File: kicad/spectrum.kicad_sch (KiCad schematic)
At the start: 114 parts

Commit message: Pre-amplifier
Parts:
- added C? (x3): 0.1uF, symbol Device:C_Small
- added C? (x3): 470uF, symbol Device:C_Polarized_Small_US
- added C?: 10uF, symbol Device:C_Small
- added R? (x4): 10K, symbol Device:R_US
- added U? (x3): Opamp_Dual, symbol Device:Opamp_Dual
- added U?: L7805, symbol Regulator_Linear:L7805
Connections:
- net +5V: now also C?.1, C?.1, C?.2, C?.2, R?.1, U?.3 (OUT), U?.8 (V+)
- net GNDREF: now also C?.1, C?.1, C?.2, C?.2, R?.2, U?.2 (GND), U?.4 (V-)
- new net: R?.1, U?.1
- new net: R?.1, R?.2, U?.2 (-)
- new net: C?.2, R?.2
- new net VDD: U?.1 (IN)
- new net VGND: C?.1, C?.1, C?.2, C?.2, R?.1, R?.2, U?.3 (+)
- new net Vin: C?.1

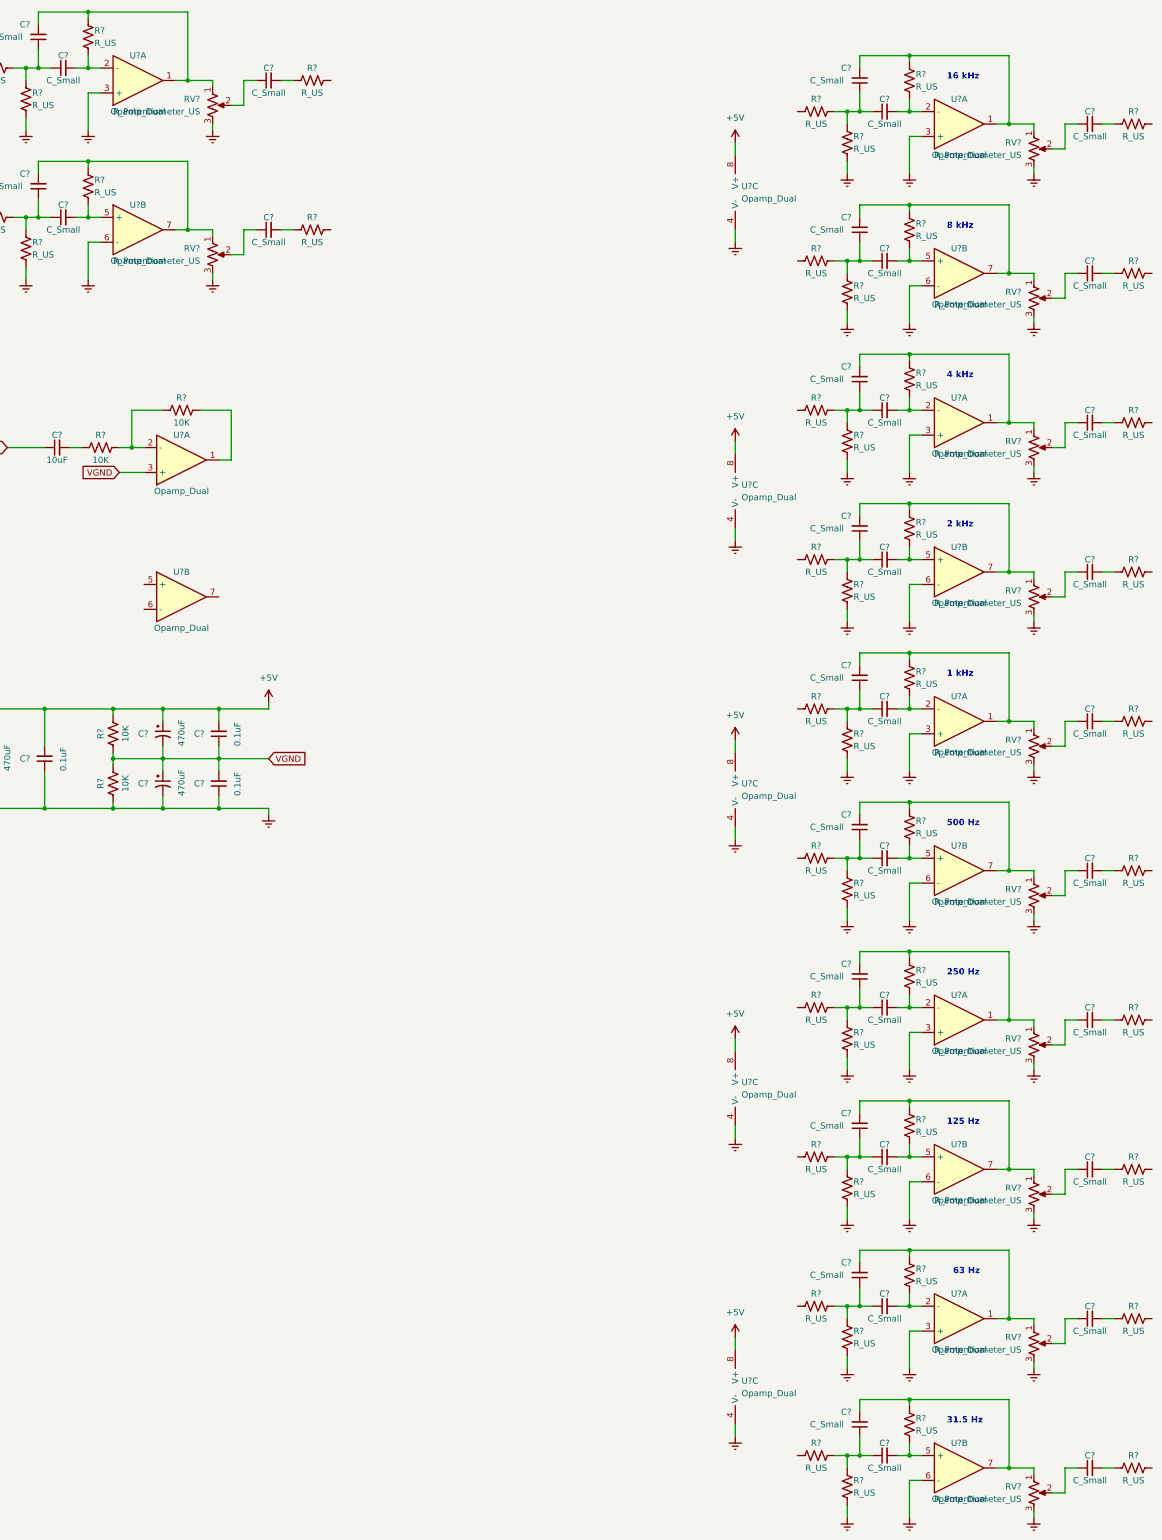
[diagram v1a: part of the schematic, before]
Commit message: Fix swapped BPF input terminals to be inverting
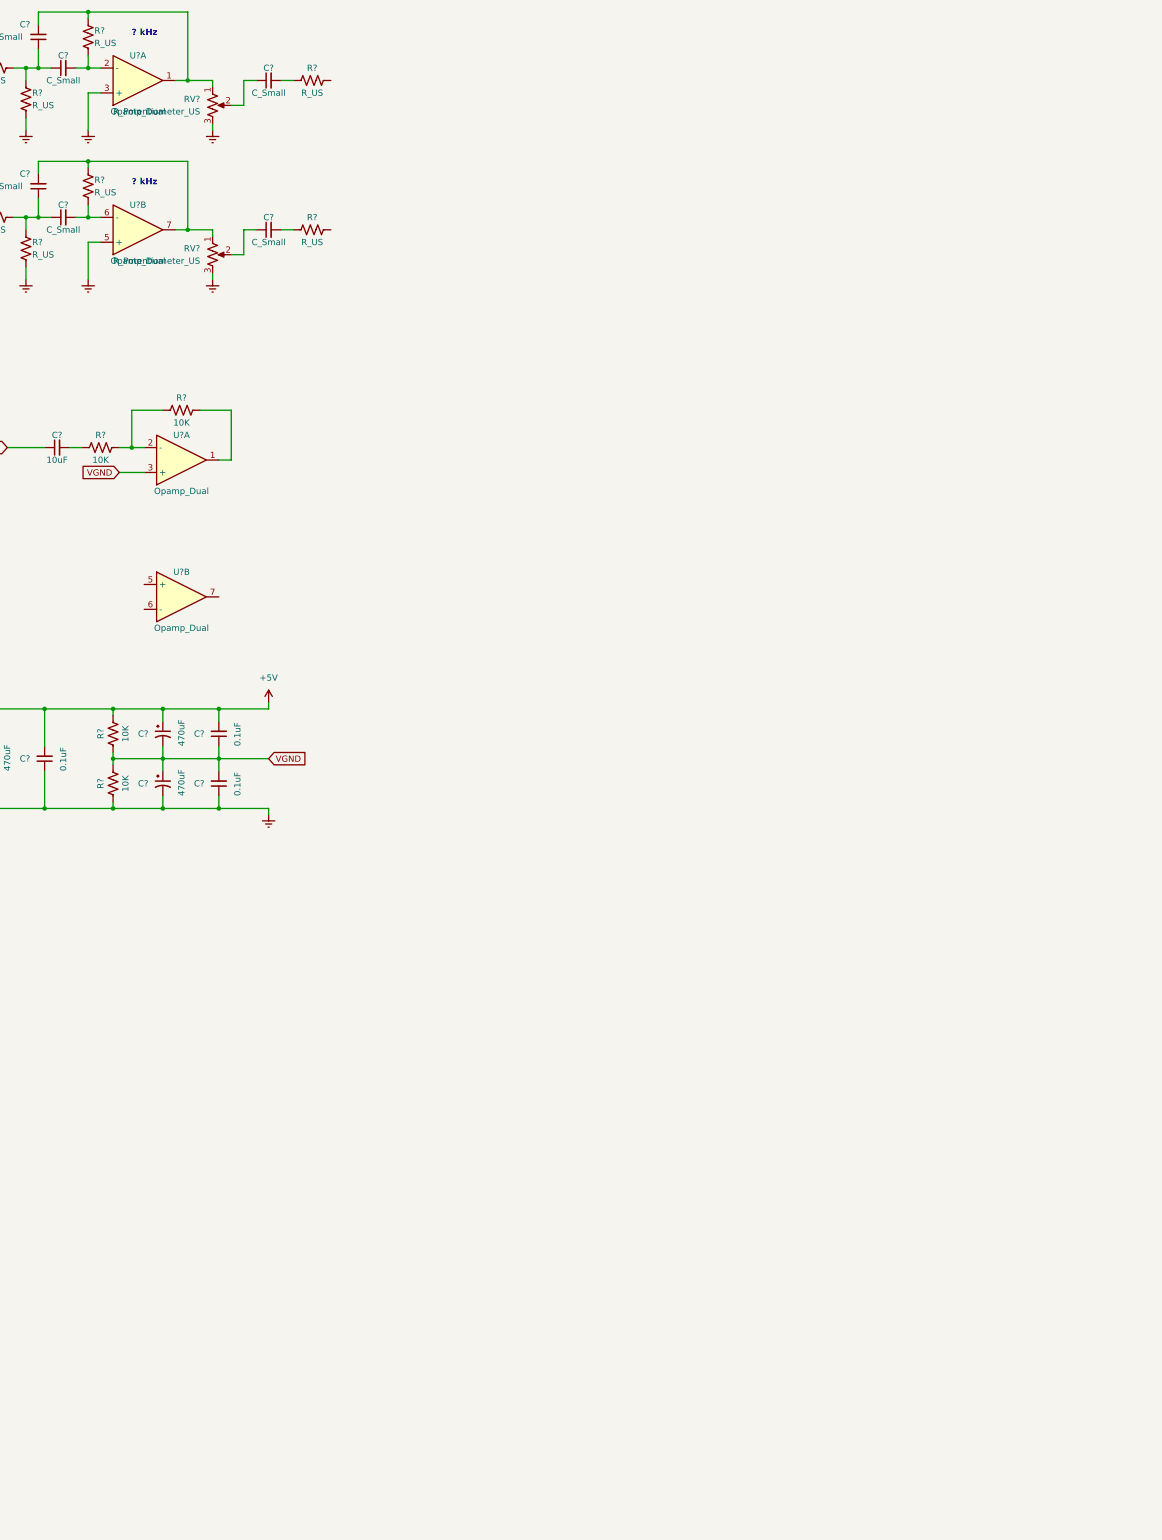
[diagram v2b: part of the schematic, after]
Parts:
- removed C? (x30): C_Small, symbol Device:C_Small
- removed R? (x40): R_US, symbol Device:R_US
- removed RV? (x10): R_Potentiometer_US, symbol Device:R_Potentiometer_US
- removed U? (x15): Opamp_Dual, symbol Device:Opamp_Dual
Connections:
- net GNDREF: now also U?.5 (+); no longer U?.6 (-)
- net at C?.2, R?.2: now also U?.6 (-); no longer U?.5 (+)
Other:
- note added: "? kHz"
- note removed: "1 kHz"
- note removed: "125 Hz"
- note removed: "16 kHz"
- note removed: "2 kHz"
- note removed: "250 Hz"
- note removed: "31.5 Hz"
- note removed: "4 kHz"
- note removed: "500 Hz"
- note removed: "63 Hz"
- note removed: "8 kHz"

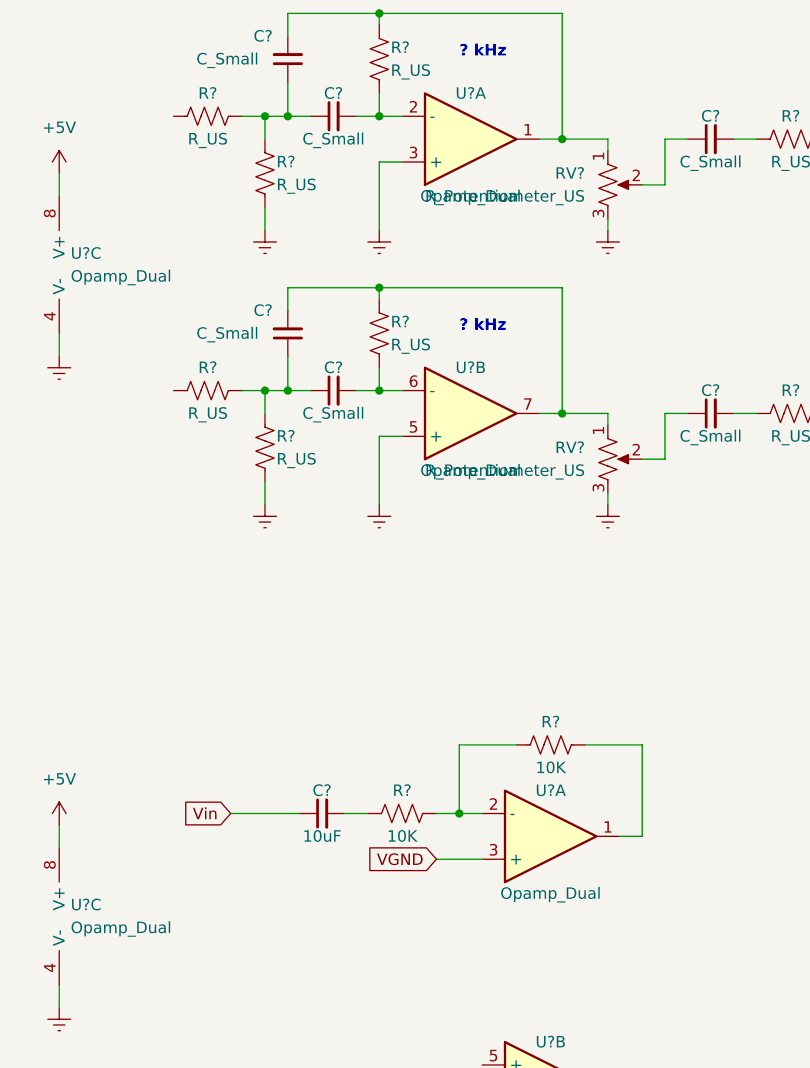
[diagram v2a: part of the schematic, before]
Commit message: Move volume POT to preamp
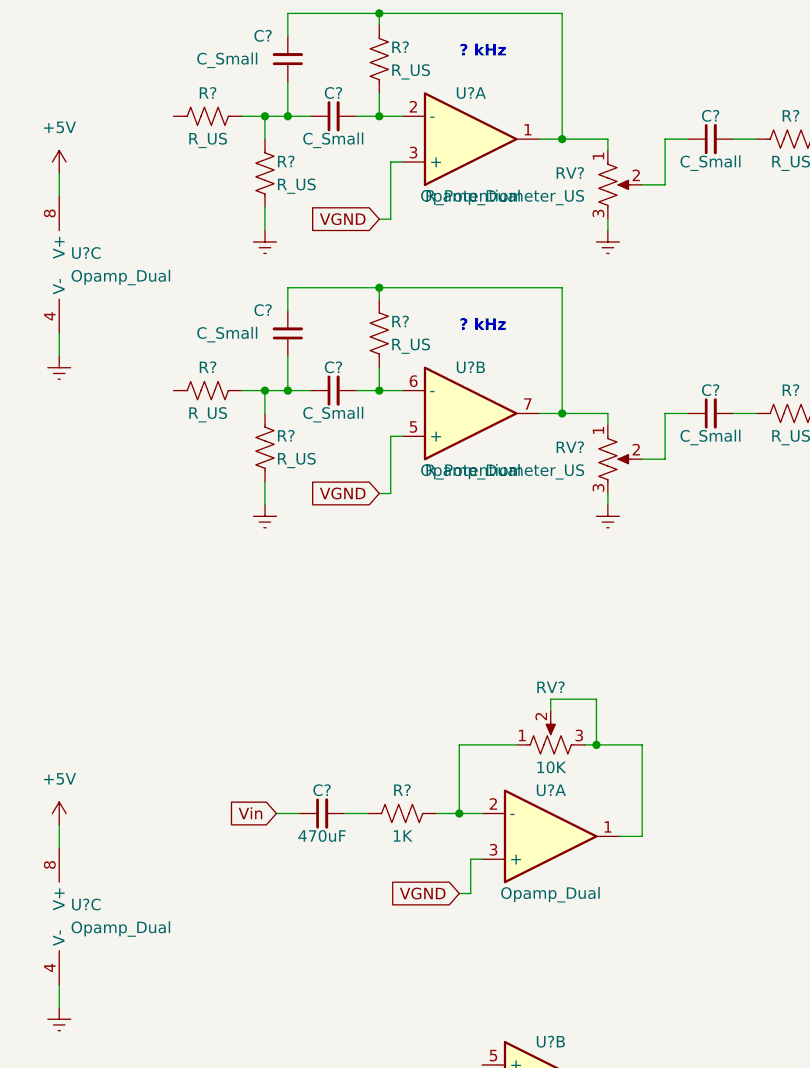
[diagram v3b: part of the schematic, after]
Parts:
- removed R?: 10K, symbol Device:R_US
- added RV?: 10K, symbol Device:R_Potentiometer_US
- C?: value 10uF -> 470uF
- R?: value 10K -> 1K
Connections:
- net GNDREF: no longer U?.3 (+), U?.5 (+)
- net VGND: now also U?.3 (+), U?.5 (+)
- net at U?.1: now also RV?.2, RV?.3
- net at R?.1, U?.2 (-): now also RV?.1
